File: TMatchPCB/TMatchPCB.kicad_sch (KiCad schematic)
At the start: 28 parts, among them J1 CapPlate, J2 CapPlate, J3 BNC, J4 CapPlate, J5 CapPlate, J6 BNC, SW1 SW_SPST, SW2 SW_SPST, SW3 SW_SPST, SW4 SW_SPST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

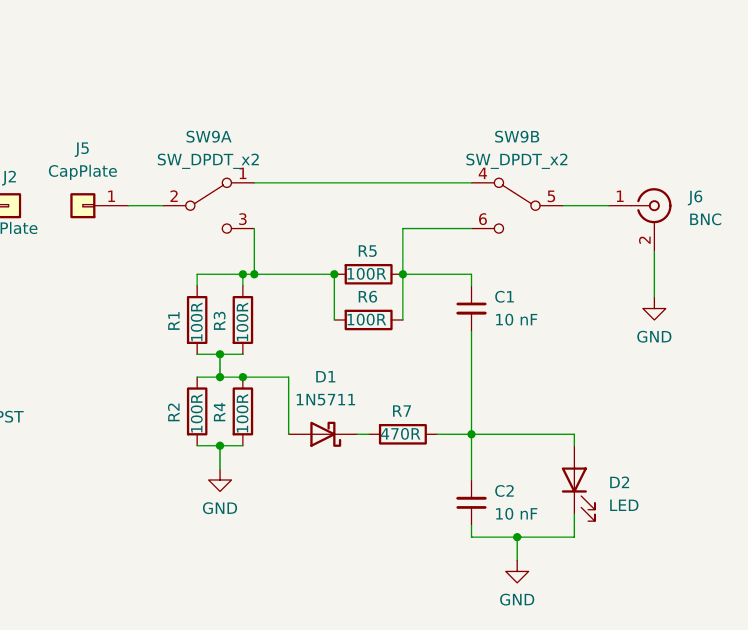
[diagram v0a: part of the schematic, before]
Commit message: Modified resistive bridge
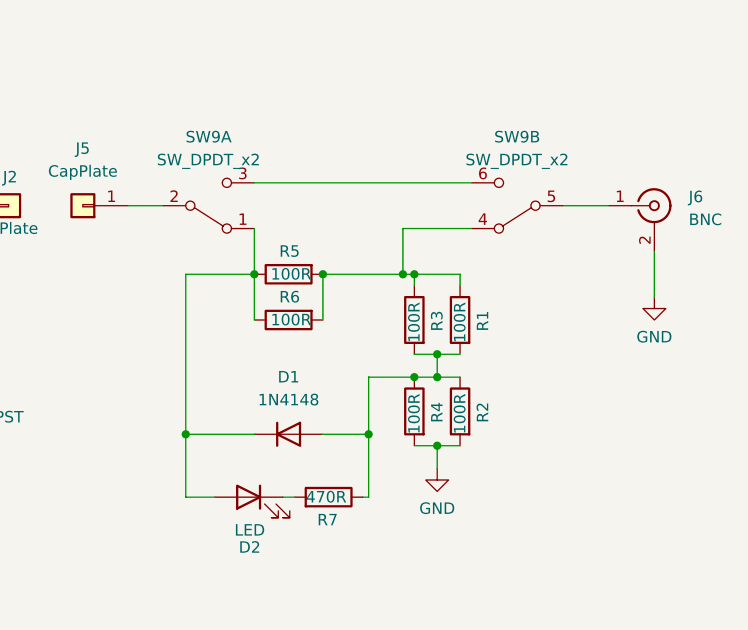
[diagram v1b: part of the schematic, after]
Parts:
- removed C1, C2: 10 nF, Capacitor_THT:C_Disc_D5.0mm_W2.5mm_P2.50mm, symbol Device:C_Small
- removed D1: 1N5711, Diode_THT:D_DO-35_SOD27_P7.62mm_Horizontal, symbol Device:D_Schottky
- added D1: 1N4148, symbol Device:D
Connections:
- net GND: no longer D2.1 (K)
- net at R1.1, R3.1, R5.2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: now also SW9.4 (A); no longer SW9.3 (C)
- net at R1.2, R2.1, R3.2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: now also R7.1, D1.2 (A)
- net at SW9.1 (A): now also D2.2 (A), R5.1, R6.1, D1.1 (K); no longer SW9.4 (A)
- net at R7.2: now also D2.1 (K)
- new net: SW9.3 (C), SW9.6 (C)
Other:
- moved on the sheet: D2, R1, R2, R3, R4, R5, R6, R7, SW9B

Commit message: Added 2 more taps for inductor
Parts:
- removed SW1, SW2, SW3, SW4, SW5, SW6, SW7, SW8: SW_SPST, TMatchPCB:SS22, symbol Switch:SW_SPST
- added SW1, SW10, SW2, SW3, SW4, SW5, SW6, SW7, SW8, SW9: SPST23, TMatchPCB:SS22, symbol TMatchPCB:SPST23
- renumbered SW9 to SW11
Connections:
- net GND: now also SW1.2, SW10.2, SW2.2, SW3.2, SW4.2, SW5.2, SW6.2, SW7.2, SW8.2, SW9.2
- net at J1.1 (Pin_1), J2.1 (Pin_1): now also SW1.3, SW10.3, SW2.3, SW3.3, SW4.3, SW5.3, SW6.3, SW7.3, SW8.3, SW9.3

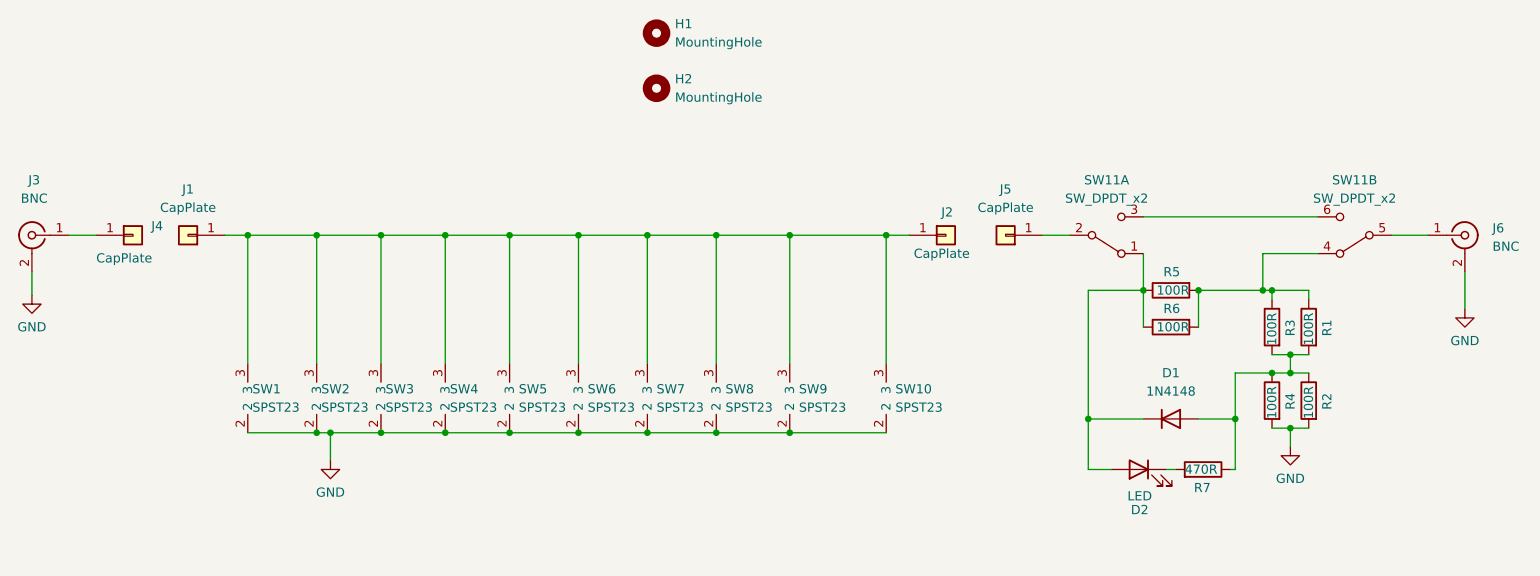
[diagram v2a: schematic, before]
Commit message: Tightened up board layout
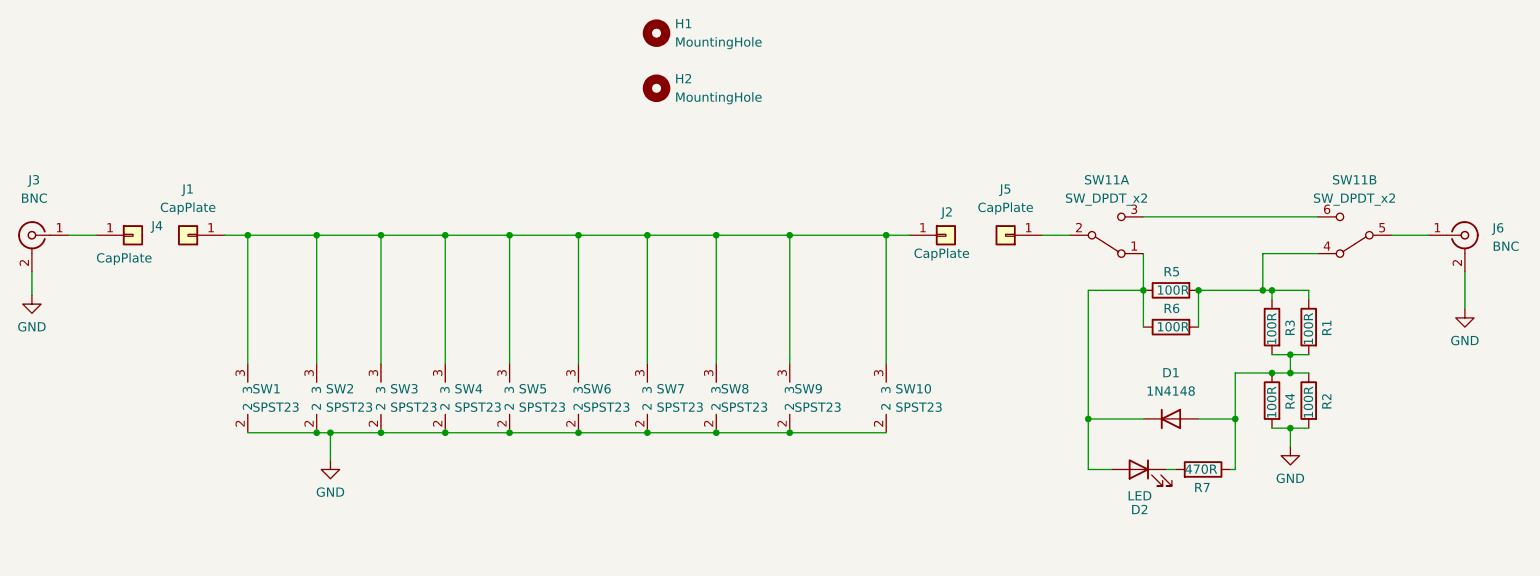
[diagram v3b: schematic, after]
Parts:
- D1: footprint (none) -> Diode_THT:D_DO-35_SOD27_P7.62mm_Horizontal
- SW1, SW10, SW2, SW3, SW4, SW5, SW6, SW7, SW8, SW9: footprint TMatchPCB:SS22 -> TMatchPCB:SS22NB
